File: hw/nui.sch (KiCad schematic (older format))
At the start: 27 parts, among them J1 D_PWR, J2 IR_RCV, J3 A_PWR, J4 Input, J5 Output, U1 Teensy-LC, U2 LM27762, U3 PGA2311

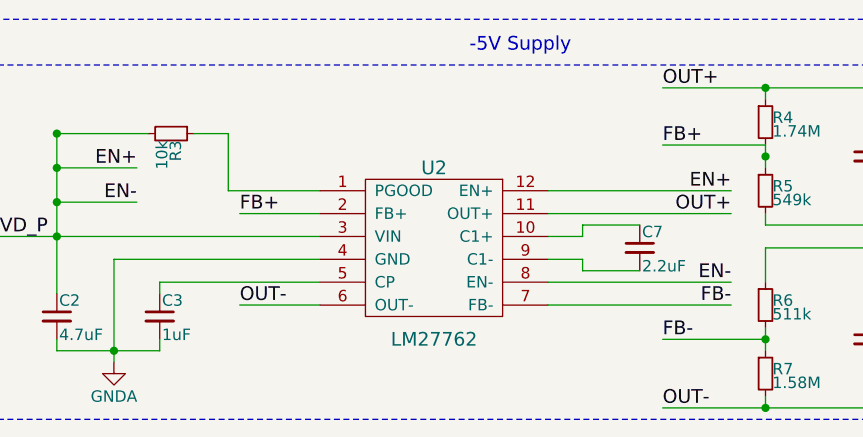
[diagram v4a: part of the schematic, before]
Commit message: Updated footprints and fixed swapped capacitors
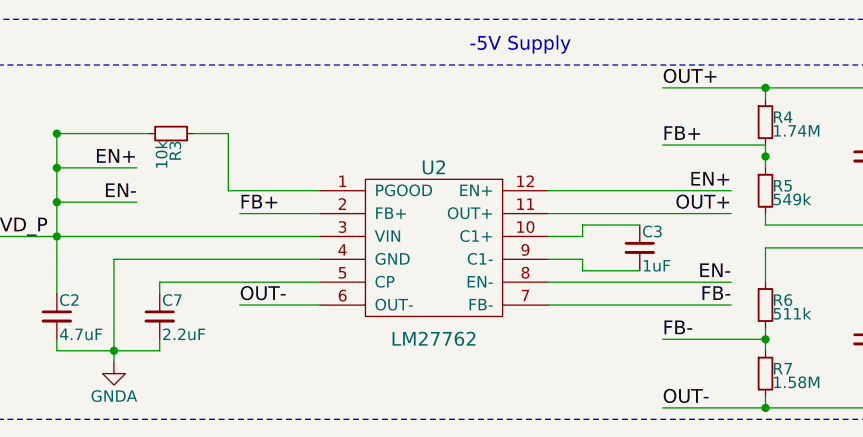
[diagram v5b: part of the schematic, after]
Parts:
- C11, C9: footprint (none) -> Capacitors_SMD:C_0603
- C2: footprint (none) -> Capacitors_SMD:C_0805
- C3: footprint (none) -> Capacitors_SMD:C_1210
- C7: footprint (none) -> Capacitors_SMD:C_0402_NoSilk
- R3, R4, R5, R6, R7: footprint (none) -> Resistors_SMD:R_0402_NoSilk
- U2: footprint (none) -> alvarop:LM27762
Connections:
- net GNDA: now also C7.2; no longer C3.2
- net at U2.10 (C1+): now also C3.1; no longer C7.1
- net at U2.5 (CP): now also C7.1; no longer C3.1
- net at U2.9 (C1-): now also C3.2; no longer C7.2
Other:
- moved on the sheet: C3, C7
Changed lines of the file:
@@
 Sheet 1 1
 Title "Nui"
-Date "2018-01-01"
-Rev "0.0.1"
+Date "2018-01-25"
+Rev "0.0.2"
 Comp "Alvaro Prieto"
 Comment1 ""
@@
 F 0 "U2" H 2700 6200 60  0000 C CNN
 F 1 "LM27762" H 2700 5450 60  0000 C CNN
-F 2 "" H 2700 5900 60  0001 C CNN
+F 2 "alvarop:LM27762" H 2700 5900 60  0001 C CNN
 F 3 "" H 2700 5900 60  0001 C CNN
 F 4 "LM27762DSST" H 2700 5850 60  0001 C CNN "MPN"
@@
 L C_Small C3
 U 1 1 5A6ABA12
-P 1500 6150
-F 0 "C3" H 1510 6220 50  0000 L CNN
-F 1 "1uF" H 1510 6070 50  0000 L CNN
-F 2 "" H 1500 6150 50  0001 C CNN
-F 3 "" H 1500 6150 50  0001 C CNN
-F 4 "ECP-U1C105MA5" H 1500 6150 60  0001 C CNN "MPN"
-	1    1500 6150
+P 3600 5850
+F 0 "C3" H 3610 5920 50  0000 L CNN
+F 1 "1uF" H 3610 5770 50  0000 L CNN
+F 2 "Capacitors_SMD:C_1210" H 3600 5850 50  0001 C CNN
+F 3 "" H 3600 5850 50  0001 C CNN
+F 4 "ECP-U1C105MA5" H 3600 5850 60  0001 C CNN "MPN"
+	1    3600 5850
 	1    0    0    -1
 $EndComp
@@
 F 0 "C2" H 1060 6220 50  0000 L CNN
 F 1 "4.7uF" H 1060 6070 50  0000 L CNN
-F 2 "" H 1050 6150 50  0001 C CNN
+F 2 "Capacitors_SMD:C_0805" H 1050 6150 50  0001 C CNN
 F 3 "" H 1050 6150 50  0001 C CNN
 F 4 "LMK212BJ475KD-T" H 1050 6150 60  0001 C CNN "MPN"
@@
 F 0 "C9" H 4610 5520 50  0000 L CNN
 F 1 "2.2uF" H 4610 5370 50  0000 L CNN
-F 2 "" H 4600 5450 50  0001 C CNN
+F 2 "Capacitors_SMD:C_0603" H 4600 5450 50  0001 C CNN
 F 3 "" H 4600 5450 50  0001 C CNN
 F 4 "C0603C225K8PACTU" H 4600 5450 60  0001 C CNN "MPN"
@@
 F 0 "C11" H 4610 6320 50  0000 L CNN
 F 1 "2.2uF" H 4610 6170 50  0000 L CNN
-F 2 "" H 4600 6250 50  0001 C CNN
+F 2 "Capacitors_SMD:C_0603" H 4600 6250 50  0001 C CNN
 F 3 "" H 4600 6250 50  0001 C CNN
 F 4 "C0603C225K8PACTU" H 4600 6250 60  0001 C CNN "MPN"
@@
 F 0 "R3" H 1580 5370 50  0000 L CNN
 F 1 "10k" H 1580 5310 50  0000 L CNN
-F 2 "" H 1550 5350 50  0001 C CNN
+F 2 "Resistors_SMD:R_0402_NoSilk" H 1550 5350 50  0001 C CNN
 F 3 "" H 1550 5350 50  0001 C CNN
 F 4 "CRCW040210K0JNEDC" H 1550 5350 60  0001 C CNN "MPN"
@@
 F 0 "R4" H 4180 5320 50  0000 L CNN
 F 1 "1.74M" H 4180 5260 50  0000 L CNN
-F 2 "" H 4150 5300 50  0001 C CNN
+F 2 "Resistors_SMD:R_0402_NoSilk" H 4150 5300 50  0001 C CNN
 F 3 "" H 4150 5300 50  0001 C CNN
 F 4 "CRCW04021M74FKED" H 4150 5300 60  0001 C CNN "MPN"
@@
 F 0 "R5" H 4180 5620 50  0000 L CNN
 F 1 "549k" H 4180 5560 50  0000 L CNN
-F 2 "" H 4150 5600 50  0001 C CNN
+F 2 "Resistors_SMD:R_0402_NoSilk" H 4150 5600 50  0001 C CNN
 F 3 "" H 4150 5600 50  0001 C CNN
 F 4 "CRCW0402549KFKED" H 4150 5600 60  0001 C CNN "MPN"
@@
 F 0 "R6" H 4180 6120 50  0000 L CNN
 F 1 "511k" H 4180 6060 50  0000 L CNN
-F 2 "" H 4150 6100 50  0001 C CNN
+F 2 "Resistors_SMD:R_0402_NoSilk" H 4150 6100 50  0001 C CNN
 F 3 "" H 4150 6100 50  0001 C CNN
 F 4 "CRCW0402511KFKED" H 4150 6100 60  0001 C CNN "MPN"
@@
 F 0 "R7" H 4180 6420 50  0000 L CNN
 F 1 "1.58M" H 4180 6360 50  0000 L CNN
-F 2 "" H 4150 6400 50  0001 C CNN
+F 2 "Resistors_SMD:R_0402_NoSilk" H 4150 6400 50  0001 C CNN
 F 3 "" H 4150 6400 50  0001 C CNN
 F 4 "CRCW04021M58FKED" H 4150 6400 60  0001 C CNN "MPN"
@@
 L C_Small C7
 U 1 1 5A6ABF0B
-P 3600 5850
-F 0 "C7" H 3610 5920 50  0000 L CNN
-F 1 "2.2uF" H 3610 5770 50  0000 L CNN
-F 2 "" H 3600 5850 50  0001 C CNN
-F 3 "" H 3600 5850 50  0001 C CNN
-F 4 "JMK105BJ225MV-F" H 3600 5850 60  0001 C CNN "MPN"
-	1    3600 5850
+P 1500 6150
+F 0 "C7" H 1510 6220 50  0000 L CNN
+F 1 "2.2uF" H 1510 6070 50  0000 L CNN
+F 2 "Capacitors_SMD:C_0402_NoSilk" H 1500 6150 50  0001 C CNN
+F 3 "" H 1500 6150 50  0001 C CNN
+F 4 "JMK105BJ225MV-F" H 1500 6150 60  0001 C CNN "MPN"
+	1    1500 6150
 	1    0    0    -1
 $EndComp
@@
 Connection ~ 1050 5500
 $Comp
-L PWR_FLAG #FLG?
+L PWR_FLAG #FLG023
 U 1 1 5A6B3B2A
 P 4100 4050
-F 0 "#FLG?" H 4100 4125 50  0001 C CNN
+F 0 "#FLG023" H 4100 4125 50  0001 C CNN
 F 1 "PWR_FLAG" H 4100 4200 50  0000 C CNN
 F 2 "" H 4100 4050 50  0001 C CNN
@@
 $EndComp
 $Comp
-L PWR_FLAG #FLG?
+L PWR_FLAG #FLG024
 U 1 1 5A6B3B86
 P 4500 4050
-F 0 "#FLG?" H 4500 4125 50  0001 C CNN
+F 0 "#FLG024" H 4500 4125 50  0001 C CNN
 F 1 "PWR_FLAG" H 4500 4200 50  0000 C CNN
 F 2 "" H 4500 4050 50  0001 C CNN

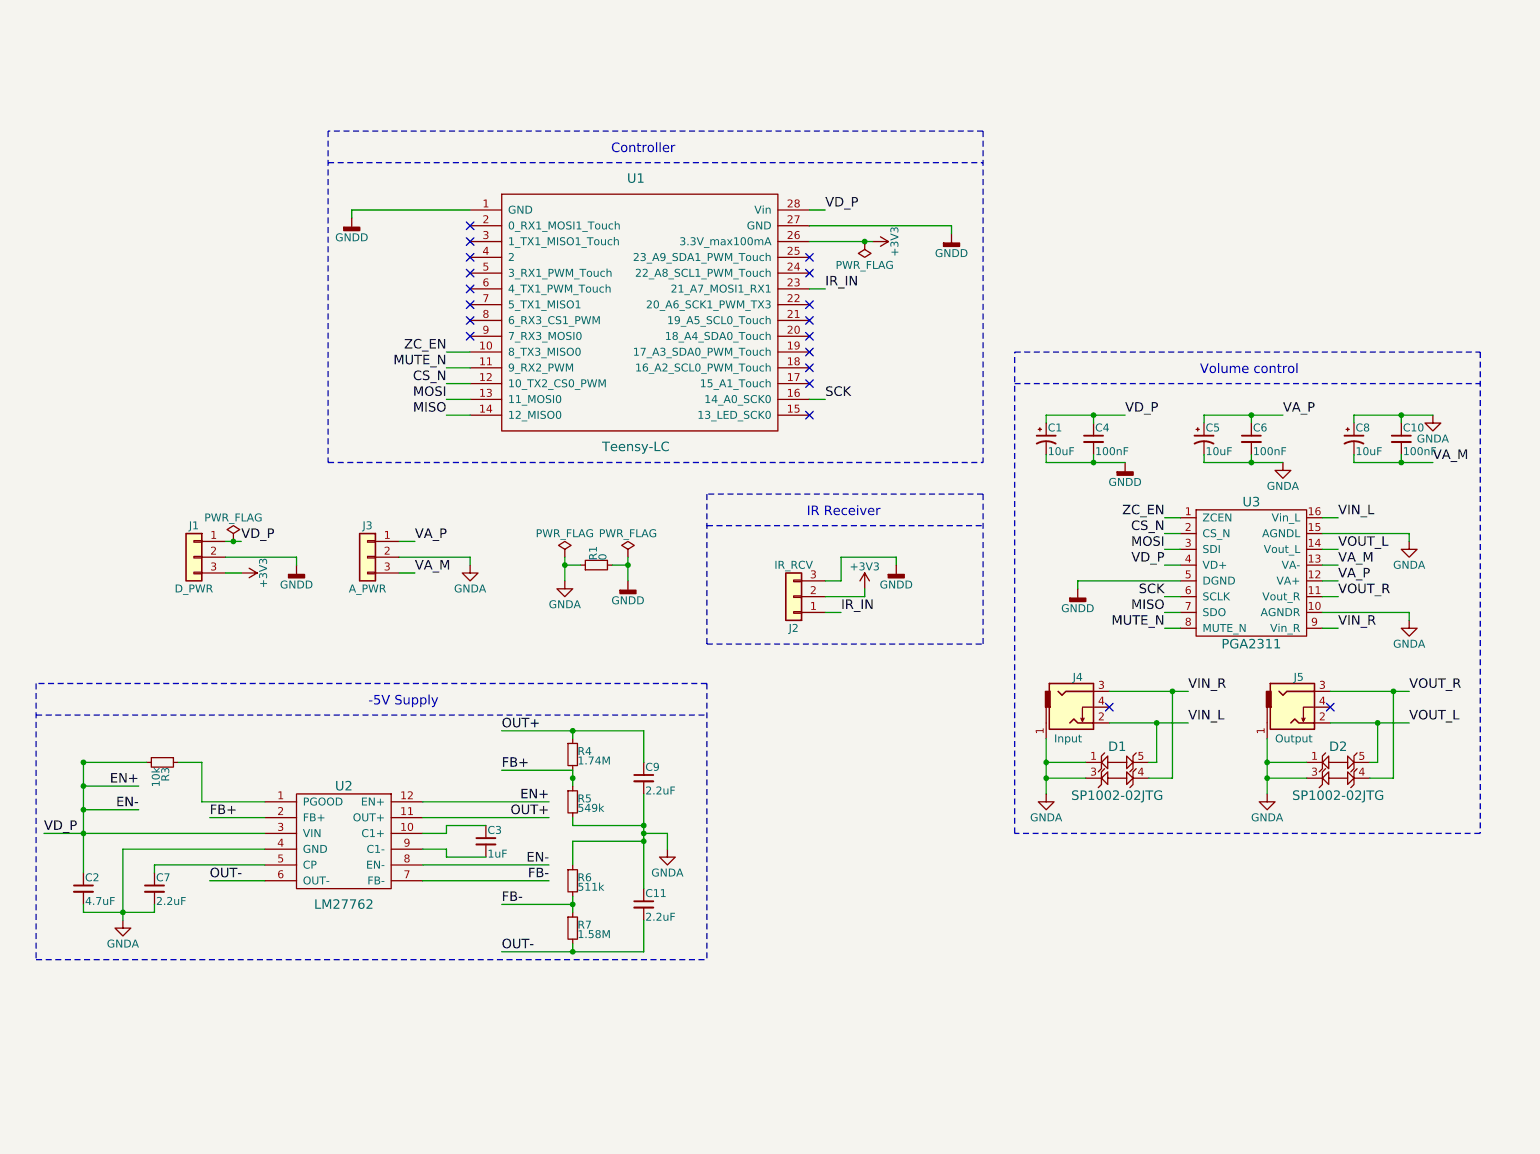
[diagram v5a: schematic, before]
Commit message: Update Nui 1.0.0 to use nrf52810 and LM27762
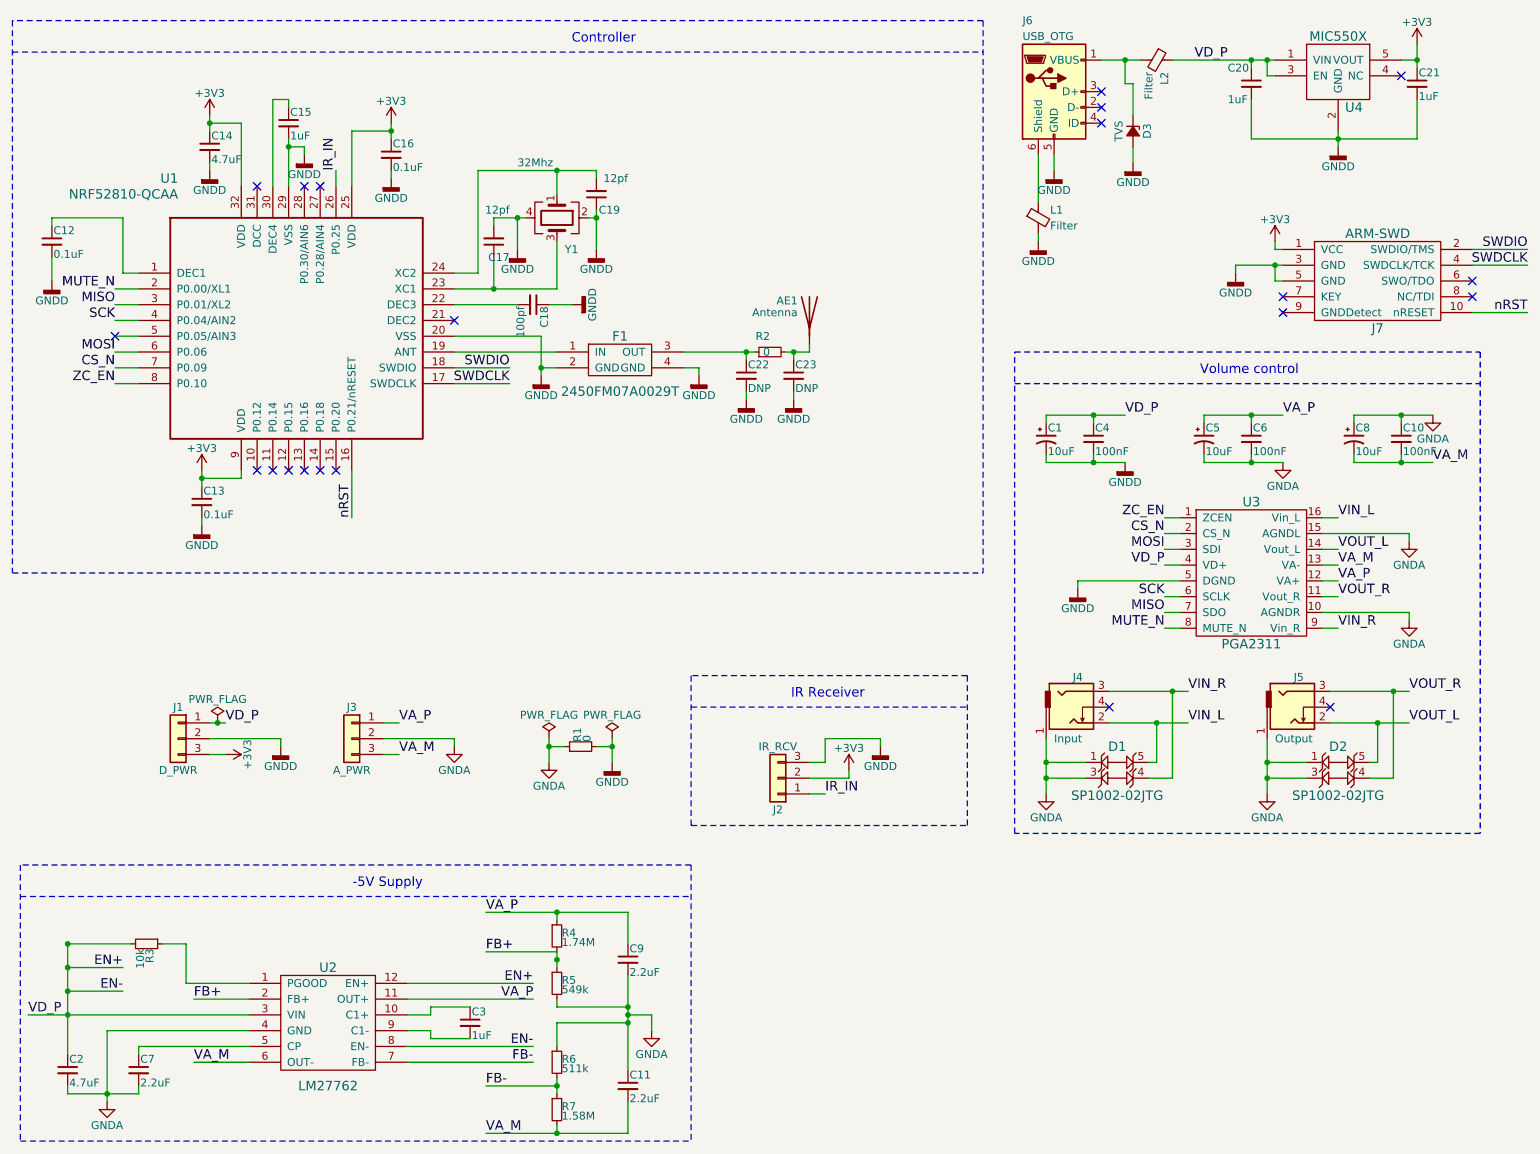
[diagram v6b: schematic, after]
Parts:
- removed U1: Teensy-LC, alvarop:Teensy-LC, symbol Teensy-LC
- added AE1: Antenna, alvarop:AMCA31-2R450G-S1F-T3, symbol Antenna
- added C12, C13, C16: 0.1uF, Capacitors_SMD:C_0603, symbol C_Small
- added C14: 4.7uF, Capacitors_SMD:C_0603, symbol C_Small
- added C15, C20, C21: 1uF, Capacitors_SMD:C_0603, symbol C_Small
- added C17, C19: 12pf, Capacitors_SMD:C_0603, symbol C_Small
- added C18: 100pf, Capacitors_SMD:C_0603, symbol C_Small
- added C22, C23: DNP, Capacitors_SMD:C_0402_NoSilk, symbol C_Small
- added D3: TVS, Diodes_SMD:D_0603, symbol D_Zener_Small_ALT
- added F1: 2450FM07A0029T, alvarop:2450FM07A0029T, symbol 2450FM07A0029T
- added J6: USB_OTG, alvarop:USB_MICRO_B, symbol USB_OTG
- added J7: ARM-SWD, alvarop:ARM_SWD_SMD, symbol ARM-SWD
- added L1, L2: Filter, Resistors_SMD:R_0603, symbol Ferrite_Bead_Small
- added R2: 0, Resistors_SMD:R_0402_NoSilk, symbol R_Small
- added U1: NRF52810-QCAA, alvarop:NRF52810_QCAA_QFN32, symbol NRF52810-QCAA
- added U4: MIC550X, alvarop:SOT-23(M5), symbol MIC550X
- added Y1: 32Mhz, Crystals:Crystal_SMD_2016-4pin_2.0x1.6mm, symbol Crystal_GND24
- R1: footprint Capacitors_SMD:C_0603 -> Resistors_SMD:R_0603
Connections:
- net OUT+ is gone; now on net VA_P: C9.1, R4.1, U2.11 (OUT+)
- net OUT- is gone; now on net VA_M: C11.2, R7.2, U2.6 (OUT-)
- net +3V3: now also C13.1, C14.1, C16.1, C21.1, J7.1 (VCC), U1.25 (VDD), U1.32 (VDD), U1.9 (VDD), U4.5 (VOUT)
- net CS_N: now also U1.7 (P0.09)
- net EN+: now also C20.1, L2.1, U4.1 (VIN), U4.3 (EN)
- net GNDD: now also C12.2, C13.2, C14.2, C15.2, C16.2, C17.2, C18.1, C19.1, C20.2, C21.2, C22.2, C23.2, D3.2 (A), F1.2 (GND), F1.4 (GND), J6.5 (GND), J7.3 (GND), J7.5 (GND), L1.2, U1.20 (VSS), U1.29 (VSS), U4.2 (GND), Y1.2, Y1.4
- net IR_IN: now also U1.26 (P0.25)
- net MISO: now also U1.3 (P0.01/XL2)
- net MOSI: now also U1.6 (P0.06)
- net MUTE_N: now also U1.2 (P0.00/XL1)
- net SCK: now also U1.4 (P0.04/AIN2)
- net ZC_EN: now also U1.8 (P0.10)
- new net: C12.1, U1.1 (DEC1)
- new net: F1.1 (IN), U1.19 (ANT)
- new net: C18.2, U1.22 (DEC3)
- new net: C17.1, U1.23 (XC1), Y1.3
- new net: C19.2, U1.24 (XC2), Y1.1
- new net: C15.1, U1.30 (DEC4)
- new net: D3.1 (K), J6.1 (VBUS), L2.2
- new net: J6.6 (Shield), L1.1
- new net: C22.1, F1.3 (OUT), R2.1
- new net: AE1.1 (A), C23.1, R2.2
- new net SWDCLK: J7.4 (SWDCLK/TCK), U1.17 (SWDCLK)
- new net SWDIO: J7.2 (SWDIO/TMS), U1.18 (SWDIO)
- new net nRST: J7.10 (nRESET), U1.16 (P0.21/nRESET)
- no-connect marks 19 -> 21
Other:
- moved on the sheet: C11, C2, C3, C7, C9, J1, J2, J3, R1, R3, R4, R5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
